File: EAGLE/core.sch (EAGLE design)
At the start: 46 parts, among them IC1 MCP1825S-3302E, Q1 MMDT3904, U3 STM32F10XCXT6, U4 SST25VF040B-Q, X1 USB-MICROB, X2 IPEX-20279-001E, Y1 8Mhz, Y2 32Khz

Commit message: Updated schematic after initial review
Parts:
- removed C12: 10uF, SparkFun:CAP_POL1206
- U4: value SST25VF040B-Q -> SST25VF040B-S2; device Spark:SST25VF040B-Q -> Spark:SST25VF040B-S2
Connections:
- net GND: no longer C12.-
- net VDDA: no longer C12.+
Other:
- moved on the sheet: C13, C14, C15, L2, Y2
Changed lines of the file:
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@@
 <part name="+3V2" library="supply1" deviceset="+3V3" device=""/>
 <part name="GND13" library="SparkFun" deviceset="GND" device=""/>
-<part name="U4" library="Spark" deviceset="SST25VF040B" device="-Q"/>
+<part name="U4" library="Spark" deviceset="SST25VF040B" device="-S2" value="SST25VF040B-S2"/>
 <part name="+3V12" library="supply1" deviceset="+3V3" device=""/>
 <part name="GND22" library="supply1" deviceset="GND" device=""/>
@@
 <part name="C6" library="rcl" deviceset="C-EU" device="C0603" value="100nF"/>
 <part name="VDDA" library="supply2" deviceset="VCC" device=""/>
-<part name="C12" library="SparkFun" deviceset="CAP_POL" device="1206" value="10uF"/>
 <part name="C13" library="rcl" deviceset="C-EU" device="C0603" value="100nF"/>
-<part name="GND14" library="supply1" deviceset="GND" device=""/>
 <part name="GND18" library="supply1" deviceset="GND" device=""/>
 <part name="+3V3" library="supply1" deviceset="+3V3" device=""/>
@@
 <text x="226.06" y="40.64" size="1.778" layer="97">Wi-Fi Module</text>
 <text x="396.24" y="123.19" size="1.778" layer="91">VDDA</text>
-<text x="494.03" y="162.56" size="1.778" layer="91">VDDA</text>
+<text x="474.98" y="173.99" size="1.778" layer="91">VDDA</text>
 </plain>
 <instances>
@@
 </instance>
 <instance part="VDDA" gate="G$1" x="398.78" y="119.38" smashed="yes"/>
-<instance part="C12" gate="G$1" x="481.33" y="142.24"/>
-<instance part="C13" gate="G$1" x="491.49" y="142.24" smashed="yes">
-<attribute name="NAME" x="493.014" y="142.621" size="1.778" layer="95"/>
-<attribute name="VALUE" x="493.014" y="137.541" size="1.778" layer="96"/>
-</instance>
-<instance part="GND14" gate="1" x="481.33" y="130.81"/>
-<instance part="GND18" gate="1" x="491.49" y="130.81"/>
-<instance part="+3V3" gate="G$1" x="452.12" y="151.13" smashed="yes" rot="R90">
-<attribute name="VALUE" x="444.5" y="151.13" size="1.778" layer="96"/>
-</instance>
-<instance part="VDDA1" gate="G$1" x="496.57" y="158.75" smashed="yes"/>
-<instance part="L2" gate="G$1" x="468.63" y="151.13" rot="R90"/>
+<instance part="C13" gate="G$1" x="488.95" y="144.78" smashed="yes">
+<attribute name="NAME" x="490.474" y="145.161" size="1.778" layer="95"/>
+<attribute name="VALUE" x="490.474" y="140.081" size="1.778" layer="96"/>
+</instance>
+<instance part="GND18" gate="1" x="488.95" y="133.35"/>
+<instance part="+3V3" gate="G$1" x="488.95" y="172.72" smashed="yes">
+<attribute name="VALUE" x="488.95" y="180.34" size="1.778" layer="96" rot="R270"/>
+</instance>
+<instance part="VDDA1" gate="G$1" x="477.52" y="170.18" smashed="yes"/>
+<instance part="L2" gate="G$1" x="488.95" y="160.02"/>
 <instance part="R4" gate="G$1" x="82.55" y="38.1" smashed="yes" rot="R180">
 <attribute name="NAME" x="80.01" y="39.878" size="1.778" layer="95"/>
 <attribute name="VALUE" x="80.01" y="34.798" size="1.778" layer="96"/>
 </instance>
-<instance part="GND19" gate="1" x="430.53" y="135.89" rot="R270"/>
-<instance part="Y2" gate="G$1" x="448.31" y="135.89" smashed="yes" rot="R90">
-<attribute name="NAME" x="446.786" y="140.208" size="1.778" layer="95"/>
-<attribute name="VALUE" x="445.262" y="129.54" size="1.778" layer="96"/>
-</instance>
-<instance part="C14" gate="G$1" x="440.69" y="140.97" smashed="yes" rot="R270">
-<attribute name="NAME" x="437.388" y="143.129" size="1.778" layer="95"/>
-<attribute name="VALUE" x="436.626" y="145.796" size="1.778" layer="96"/>
-</instance>
-<instance part="C15" gate="G$1" x="440.69" y="130.81" smashed="yes" rot="R270">
-<attribute name="NAME" x="437.388" y="126.238" size="1.778" layer="95"/>
-<attribute name="VALUE" x="436.118" y="123.19" size="1.778" layer="96"/>
+<instance part="GND19" gate="1" x="430.53" y="139.7" rot="R270"/>
+<instance part="Y2" gate="G$1" x="448.31" y="139.7" smashed="yes" rot="R90">
+<attribute name="NAME" x="446.786" y="144.018" size="1.778" layer="95"/>
+<attribute name="VALUE" x="445.262" y="133.35" size="1.778" layer="96"/>
+</instance>
+<instance part="C14" gate="G$1" x="440.69" y="144.78" smashed="yes" rot="R270">
+<attribute name="NAME" x="437.388" y="146.939" size="1.778" layer="95"/>
+<attribute name="VALUE" x="436.626" y="149.606" size="1.778" layer="96"/>
+</instance>
+<instance part="C15" gate="G$1" x="440.69" y="134.62" smashed="yes" rot="R270">
+<attribute name="NAME" x="437.388" y="130.048" size="1.778" layer="95"/>
+<attribute name="VALUE" x="436.118" y="127" size="1.778" layer="96"/>
 </instance>
 <instance part="IC1" gate="G$1" x="59.69" y="160.02"/>
@@
 </segment>
 <segment>
-<pinref part="C12" gate="G$1" pin="-"/>
-<wire x1="481.33" y1="137.16" x2="481.33" y2="133.35" width="0.1524" layer="91"/>
-<pinref part="GND14" gate="1" pin="GND"/>
-</segment>
-<segment>
 <pinref part="C13" gate="G$1" pin="2"/>
 <pinref part="GND18" gate="1" pin="GND"/>
-<wire x1="491.49" y1="137.16" x2="491.49" y2="133.35" width="0.1524" layer="91"/>
-</segment>
-<segment>
-<wire x1="435.61" y1="140.97" x2="435.61" y2="135.89" width="0.1524" layer="91"/>
-<wire x1="435.61" y1="135.89" x2="435.61" y2="130.81" width="0.1524" layer="91"/>
-<wire x1="433.07" y1="135.89" x2="435.61" y2="135.89" width="0.1524" layer="91"/>
-<junction x="435.61" y="135.89"/>
+<wire x1="488.95" y1="139.7" x2="488.95" y2="135.89" width="0.1524" layer="91"/>
+</segment>
+<segment>
+<wire x1="435.61" y1="144.78" x2="435.61" y2="139.7" width="0.1524" layer="91"/>
+<wire x1="435.61" y1="139.7" x2="435.61" y2="134.62" width="0.1524" layer="91"/>
+<wire x1="433.07" y1="139.7" x2="435.61" y2="139.7" width="0.1524" layer="91"/>
+<junction x="435.61" y="139.7"/>
 <pinref part="C14" gate="G$1" pin="2"/>
 <pinref part="C15" gate="G$1" pin="2"/>
@@
 </segment>
 <segment>
-<wire x1="461.01" y1="151.13" x2="454.66" y2="151.13" width="0.1524" layer="91"/>
-<pinref part="+3V3" gate="G$1" pin="+3V3"/>
-<pinref part="L2" gate="G$1" pin="1"/>
-</segment>
-<segment>
 <pinref part="LED_RGB" gate="G$1" pin="A2"/>
 <pinref part="+3V9" gate="G$1" pin="+3V3"/>
 <wire x1="342.9" y1="71.12" x2="336.55" y2="71.12" width="0.1524" layer="91"/>
 <wire x1="336.55" y1="71.12" x2="336.55" y2="80.01" width="0.1524" layer="91"/>
+</segment>
+<segment>
+<pinref part="+3V3" gate="G$1" pin="+3V3"/>
+<pinref part="L2" gate="G$1" pin="1"/>
+<wire x1="488.95" y1="170.18" x2="488.95" y2="167.64" width="0.1524" layer="91"/>
 </segment>
 </net>
@@
 </segment>
 <segment>
-<pinref part="C12" gate="G$1" pin="+"/>
-<wire x1="476.25" y1="151.13" x2="481.33" y2="151.13" width="0.1524" layer="91"/>
-<wire x1="481.33" y1="151.13" x2="481.33" y2="144.78" width="0.1524" layer="91"/>
 <pinref part="C13" gate="G$1" pin="1"/>
-<wire x1="491.49" y1="144.78" x2="491.49" y2="151.13" width="0.1524" layer="91"/>
-<wire x1="491.49" y1="151.13" x2="481.33" y2="151.13" width="0.1524" layer="91"/>
-<junction x="481.33" y="151.13"/>
-<wire x1="491.49" y1="151.13" x2="496.57" y2="151.13" width="0.1524" layer="91"/>
-<junction x="491.49" y="151.13"/>
-<wire x1="496.57" y1="151.13" x2="496.57" y2="156.21" width="0.1524" layer="91"/>
+<wire x1="488.95" y1="147.32" x2="488.95" y2="149.86" width="0.1524" layer="91"/>
+<wire x1="488.95" y1="149.86" x2="477.52" y2="149.86" width="0.1524" layer="91"/>
+<wire x1="477.52" y1="149.86" x2="477.52" y2="167.64" width="0.1524" layer="91"/>
 <pinref part="VDDA1" gate="G$1" pin="VCC"/>
 <pinref part="L2" gate="G$1" pin="2"/>
+<wire x1="488.95" y1="152.4" x2="488.95" y2="149.86" width="0.1524" layer="91"/>
+<junction x="488.95" y="149.86"/>
 </segment>
 </net>
@@
 <segment>
 <pinref part="C14" gate="G$1" pin="1"/>
-<wire x1="443.23" y1="140.97" x2="448.31" y2="140.97" width="0.1524" layer="91"/>
+<wire x1="443.23" y1="144.78" x2="448.31" y2="144.78" width="0.1524" layer="91"/>
 <pinref part="Y2" gate="G$1" pin="2"/>
-<wire x1="448.31" y1="140.97" x2="466.09" y2="140.97" width="0.1524" layer="91"/>
-<wire x1="448.31" y1="138.43" x2="448.31" y2="140.97" width="0.1524" layer="91"/>
-<junction x="448.31" y="140.97"/>
-<label x="452.12" y="140.97" size="1.778" layer="95"/>
+<wire x1="448.31" y1="144.78" x2="466.09" y2="144.78" width="0.1524" layer="91"/>
+<wire x1="448.31" y1="142.24" x2="448.31" y2="144.78" width="0.1524" layer="91"/>
+<junction x="448.31" y="144.78"/>
+<label x="452.12" y="144.78" size="1.778" layer="95"/>
 </segment>
 </net>
@@
 <segment>
 <pinref part="C15" gate="G$1" pin="1"/>
-<wire x1="443.23" y1="130.81" x2="448.31" y2="130.81" width="0.1524" layer="91"/>
+<wire x1="443.23" y1="134.62" x2="448.31" y2="134.62" width="0.1524" layer="91"/>
 <pinref part="Y2" gate="G$1" pin="1"/>
-<wire x1="448.31" y1="130.81" x2="466.09" y2="130.81" width="0.1524" layer="91"/>
-<wire x1="448.31" y1="133.35" x2="448.31" y2="130.81" width="0.1524" layer="91"/>
-<junction x="448.31" y="130.81"/>
-<label x="452.12" y="130.81" size="1.778" layer="95"/>
-</segment>
-</net>
+<wire x1="448.31" y1="134.62" x2="466.09" y2="134.62" width="0.1524" layer="91"/>
+<wire x1="448.31" y1="137.16" x2="448.31" y2="134.62" width="0.1524" layer="91"/>
+<junction x="448.31" y="134.62"/>
+<label x="452.12" y="134.62" size="1.778" layer="95"/>
+</segment>
+</net>

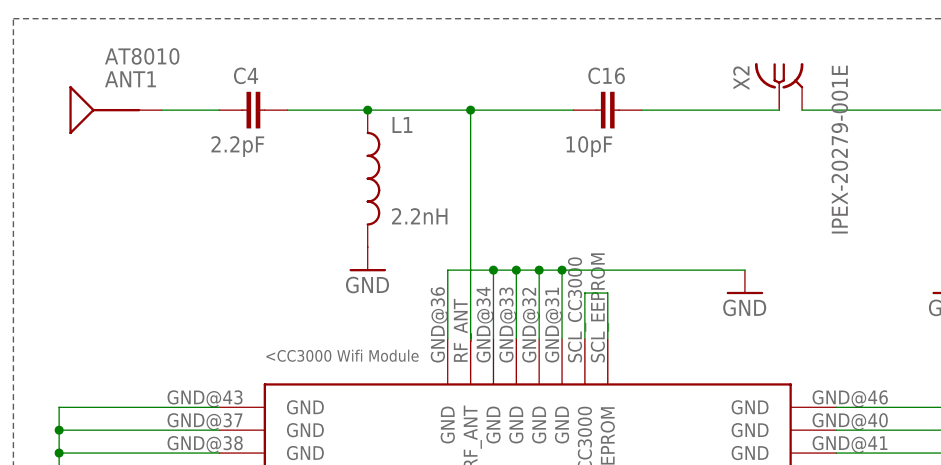
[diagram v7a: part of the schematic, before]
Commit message: Proposed RF layout.
Added C12 and overlay common pad with C16.
Added top ground plane - extended back under CC3000
Moved Antenna closer to centre line of module.
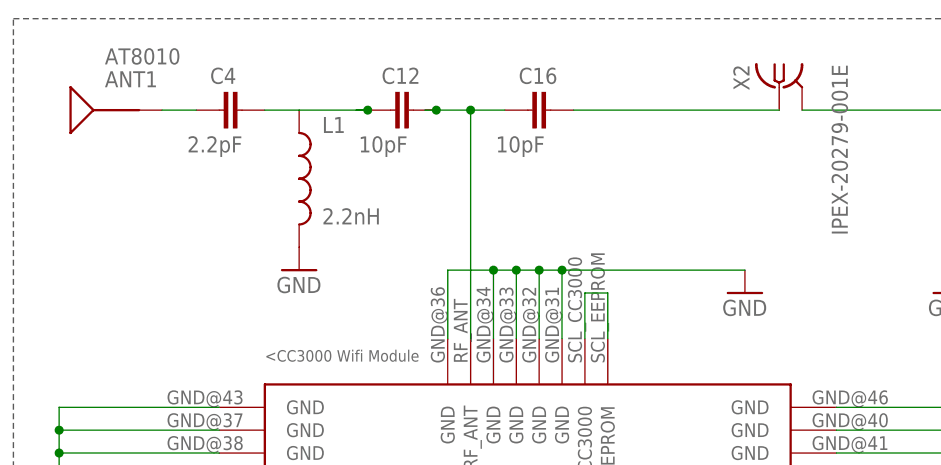
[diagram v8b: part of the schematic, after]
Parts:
- added C12: 10pF, rcl:C-EUC0603
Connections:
- new net N$5: C12.1, C4.2, L1.1
- net N$4: now also C12.2; no longer C4.2, L1.1
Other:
- moved on the sheet: C16, C4, L1
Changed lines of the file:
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@@
 <setting verticaltext="up"/>
 </settings>
-<grid distance="50" unitdist="mil" unit="mil" style="lines" multiple="1" display="yes" altdistance="0.01" altunitdist="inch" altunit="inch"/>
+<grid distance="0.1" unitdist="inch" unit="inch" style="lines" multiple="1" display="no" altdistance="0.01" altunitdist="inch" altunit="inch"/>
 <layers>
 <layer number="1" name="Top" color="4" fill="1" visible="no" active="no"/>
@@
 <layer number="91" name="Nets" color="2" fill="1" visible="yes" active="yes"/>
 <layer number="92" name="Busses" color="1" fill="1" visible="yes" active="yes"/>
-<layer number="93" name="Pins" color="2" fill="1" visible="no" active="yes"/>
+<layer number="93" name="Pins" color="2" fill="1" visible="yes" active="yes"/>
 <layer number="94" name="Symbols" color="4" fill="1" visible="yes" active="yes"/>
 <layer number="95" name="Names" color="7" fill="1" visible="yes" active="yes"/>
@@
 </class>
 <class number="1" name="vcc" width="0" drill="0">
+</class>
+<class number="2" name="RF" width="0.635" drill="0">
+<clearance class="2" value="0.762"/>
 </class>
 </classes>
@@
 <part name="GND20" library="SparkFun" deviceset="GND" device=""/>
 <part name="ANT1" library="Spark" deviceset="AT8010" device=""/>
+<part name="C12" library="rcl" deviceset="C-EU" device="C0603" value="10pF"/>
 </parts>
 <sheets>
@@
 <instance part="FRAME2" gate="G$1" x="254" y="0"/>
 <instance part="FRAME2" gate="G$2" x="401.32" y="0"/>
-<instance part="L1" gate="G$1" x="161.29" y="165.1"/>
-<instance part="C4" gate="G$1" x="147.32" y="172.72" smashed="yes" rot="R90">
-<attribute name="NAME" x="146.304" y="175.641" size="1.778" layer="95"/>
-<attribute name="VALUE" x="143.764" y="168.021" size="1.778" layer="96"/>
-</instance>
-<instance part="GND2" gate="1" x="161.29" y="154.94"/>
+<instance part="L1" gate="G$1" x="153.67" y="165.1"/>
+<instance part="C4" gate="G$1" x="144.78" y="172.72" smashed="yes" rot="R90">
+<attribute name="NAME" x="143.764" y="175.641" size="1.778" layer="95"/>
+<attribute name="VALUE" x="141.224" y="168.021" size="1.778" layer="96"/>
+</instance>
+<instance part="GND2" gate="1" x="153.67" y="154.94"/>
 <instance part="GND5" gate="1" x="203.2" y="152.4"/>
 <instance part="GND6" gate="1" x="127" y="91.44"/>
@@
 </instance>
 <instance part="X2" gate="G$1" x="207.01" y="175.26" rot="MR270"/>
-<instance part="C16" gate="G$1" x="186.69" y="172.72" smashed="yes" rot="R90">
-<attribute name="NAME" x="185.674" y="175.641" size="1.778" layer="95"/>
-<attribute name="VALUE" x="183.134" y="168.021" size="1.778" layer="96"/>
+<instance part="C16" gate="G$1" x="179.07" y="172.72" smashed="yes" rot="R90">
+<attribute name="NAME" x="178.054" y="175.641" size="1.778" layer="95"/>
+<attribute name="VALUE" x="175.514" y="168.021" size="1.778" layer="96"/>
 </instance>
 <instance part="GND20" gate="1" x="226.06" y="152.4"/>
 <instance part="ANT1" gate="G$1" x="133.35" y="172.72" rot="R90"/>
+<instance part="C12" gate="G$1" x="163.83" y="172.72" smashed="yes" rot="R90">
+<attribute name="NAME" x="162.814" y="175.641" size="1.778" layer="95"/>
+<attribute name="VALUE" x="160.274" y="168.021" size="1.778" layer="96"/>
+</instance>
 </instances>
 <busses>
@@
 </segment>
 </net>
-<net name="N$4" class="0">
+<net name="N$4" class="2">
 <segment>
 <pinref part="U2" gate="G$1" pin="RF_ANT"/>
 <wire x1="172.72" y1="147.32" x2="172.72" y2="172.72" width="0.1524" layer="91"/>
-<pinref part="C4" gate="G$1" pin="2"/>
-<wire x1="152.4" y1="172.72" x2="161.29" y2="172.72" width="0.1524" layer="91"/>
-<pinref part="L1" gate="G$1" pin="1"/>
-<wire x1="161.29" y1="172.72" x2="172.72" y2="172.72" width="0.1524" layer="91"/>
-<junction x="161.29" y="172.72"/>
 <pinref part="C16" gate="G$1" pin="1"/>
-<wire x1="184.15" y1="172.72" x2="172.72" y2="172.72" width="0.1524" layer="91"/>
+<wire x1="176.53" y1="172.72" x2="172.72" y2="172.72" width="0.1524" layer="91"/>
+<wire x1="167.64" y1="172.72" x2="168.91" y2="172.72" width="0.1524" layer="91"/>
 <junction x="172.72" y="172.72"/>
+<pinref part="C12" gate="G$1" pin="2"/>
+<wire x1="168.91" y1="172.72" x2="172.72" y2="172.72" width="0.1524" layer="91"/>
+<junction x="168.91" y="172.72"/>
 </segment>
 </net>
@@
 </segment>
 </net>
-<net name="N$2" class="0">
+<net name="N$2" class="2">
 <segment>
 <pinref part="C16" gate="G$1" pin="2"/>
 <pinref part="X2" gate="G$1" pin="1"/>
-<wire x1="191.77" y1="172.72" x2="207.01" y2="172.72" width="0.1524" layer="91"/>
-</segment>
-</net>
-<net name="N$3" class="0">
+<wire x1="184.15" y1="172.72" x2="207.01" y2="172.72" width="0.1524" layer="91"/>
+</segment>
+</net>
+<net name="N$3" class="2">
 <segment>
 <pinref part="ANT1" gate="G$1" pin="SIGNAL"/>
 <pinref part="C4" gate="G$1" pin="1"/>
-<wire x1="138.43" y1="172.72" x2="144.78" y2="172.72" width="0.1524" layer="91"/>
-</segment>
-</net>
+<wire x1="138.43" y1="172.72" x2="142.24" y2="172.72" width="0.1524" layer="91"/>
+</segment>
+</net>
+<net name="N$5" class="2">
+<segment>
+<pinref part="L1" gate="G$1" pin="1"/>
+<pinref part="C4" gate="G$1" pin="2"/>
+<wire x1="149.86" y1="172.72" x2="153.67" y2="172.72" width="0.1524" layer="91"/>
+<wire x1="160.02" y1="172.72" x2="161.29" y2="172.72" width="0.1524" layer="91"/>
+<pinref part="C12" gate="G$1" pin="1"/>
+<wire x1="161.29" y1="172.72" x2="153.67" y2="172.72" width="0.1524" layer="91"/>
+<junction x="161.29" y="172.72"/>
+</segment>
+</net>
